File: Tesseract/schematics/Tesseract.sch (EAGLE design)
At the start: 108 parts, among them IC1 MC7805CDTG, IC2 QUAD_OPAMPD, IC3 NE5532D, IC4 LM4040B10, IC5 NE5532D, Q1 SI2309CDS, Q2 BSS123, Q901 BC846

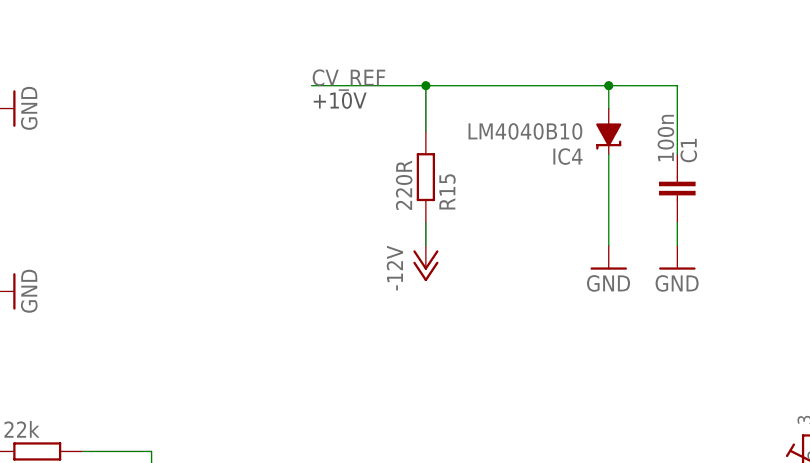
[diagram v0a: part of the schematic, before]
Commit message: changed current limiting vref resistor value to 150R
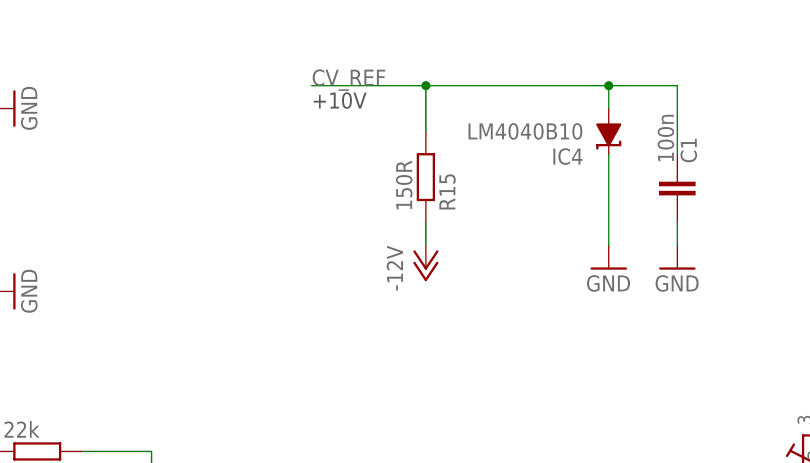
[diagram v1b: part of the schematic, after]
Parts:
- R15: value 220R -> 150R
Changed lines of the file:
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@@
 <part name="GND17" library="supply1" deviceset="GND" device=""/>
 <part name="P-2" library="supply1" deviceset="-12V" device=""/>
-<part name="R15" library="Rebel" deviceset="R-EU_" device="0603" value="220R"/>
+<part name="R15" library="Rebel" deviceset="R-EU_" device="0603" value="150R"/>
 <part name="C1" library="resistor" deviceset="C-EU" device="C0603" value="100n"/>
 <part name="GND18" library="supply1" deviceset="GND" device=""/>

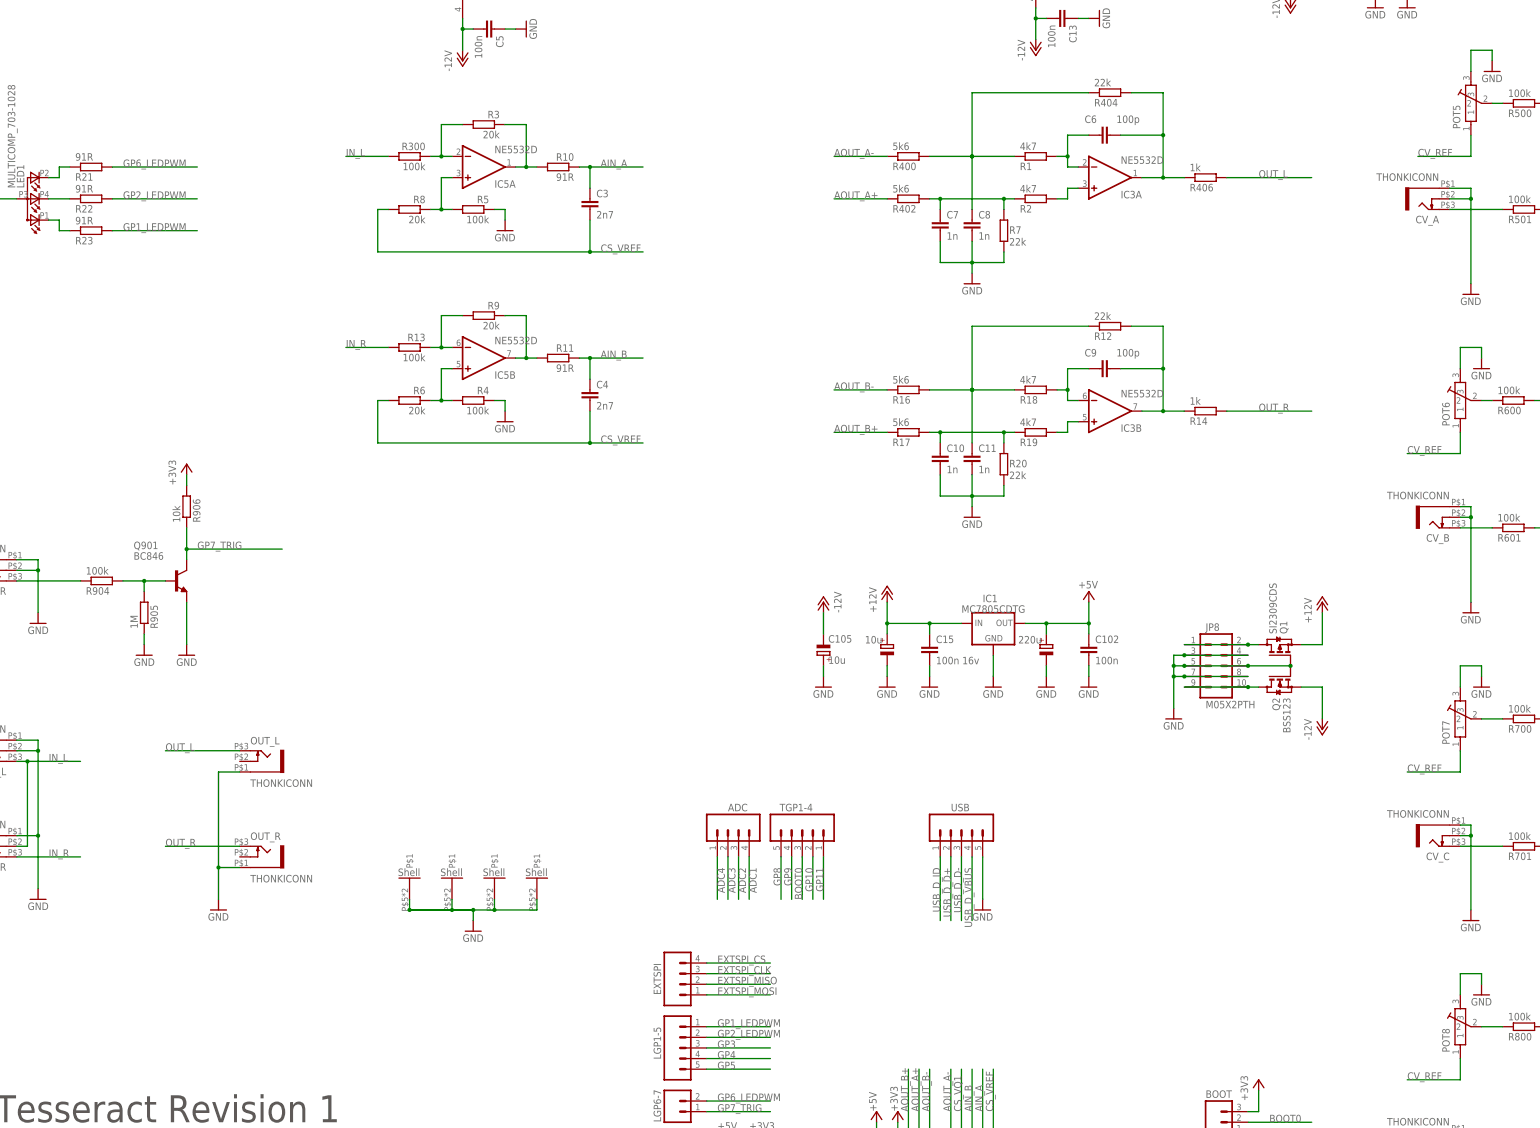
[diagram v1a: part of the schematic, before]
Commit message: component value and name changes
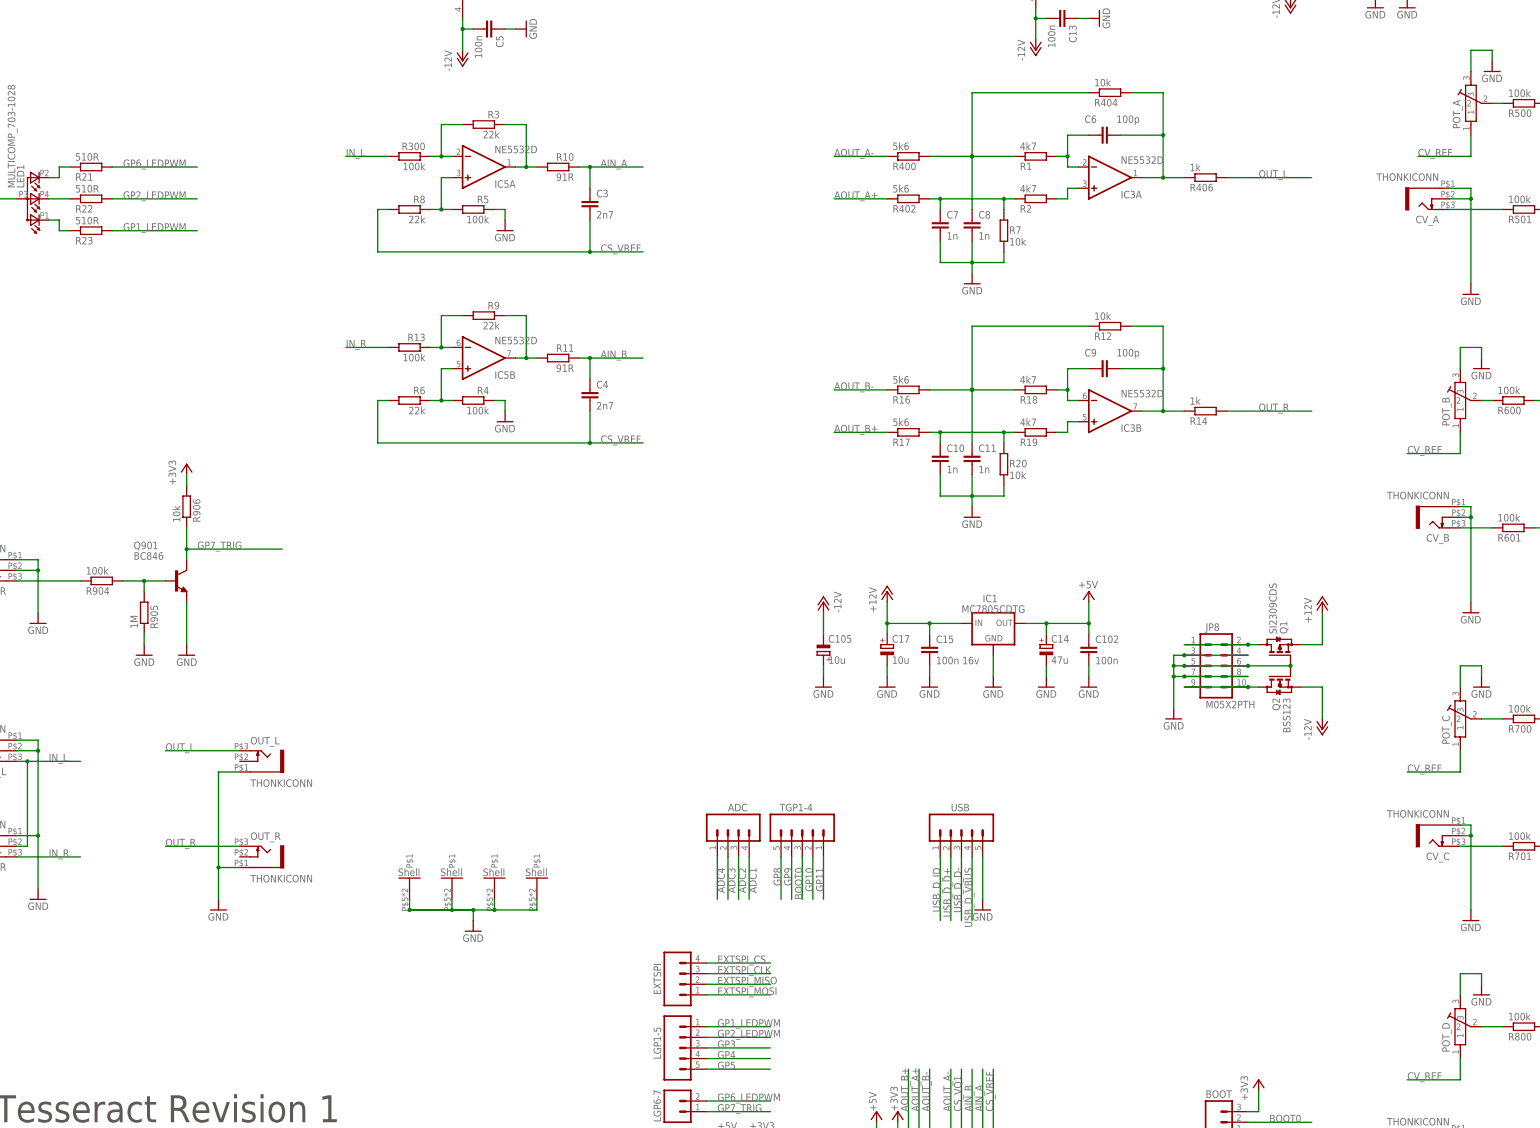
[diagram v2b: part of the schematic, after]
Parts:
- C14: value 220u -> 47u
- R12, R20, R404, R7: value 22k -> 10k
- R21, R22, R23: value 91R -> 510R
- R3, R6, R8, R9: value 20k -> 22k
- renumbered POT5 to POT_A, POT6 to POT_B, POT7 to POT_C, POT8 to POT_D

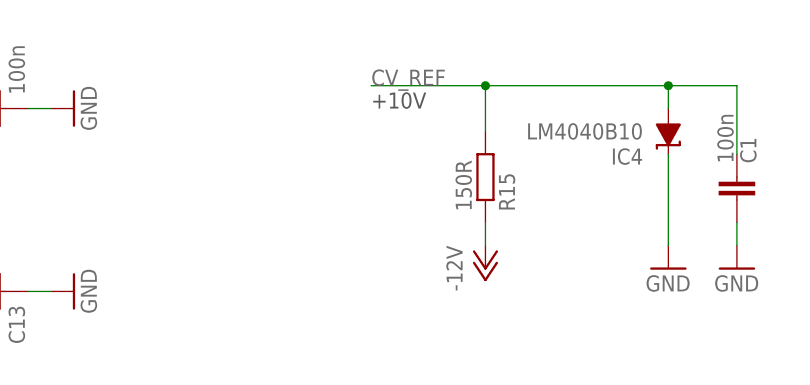
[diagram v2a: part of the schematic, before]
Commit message: corrected vref label
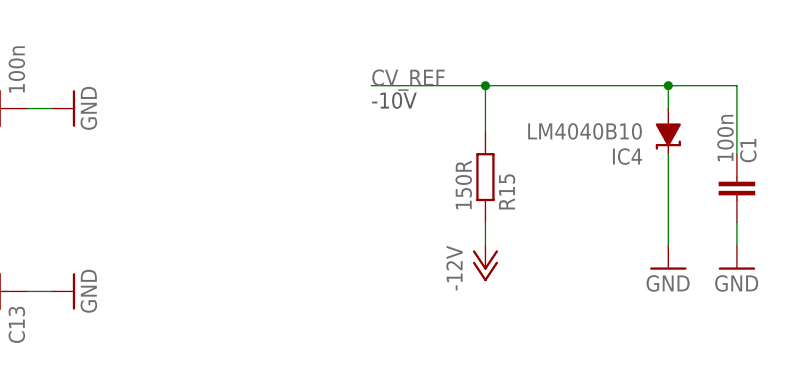
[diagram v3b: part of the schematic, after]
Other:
- note added: "-10V"
- note removed: "+10V"
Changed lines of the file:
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@@
 <text x="-66.04" y="-30.48" size="3.81" layer="97" font="vector">Copyright 2017 Rebel Technology</text>
 <text x="-66.04" y="-38.1" size="3.81" layer="97" font="vector">Published under the GNU GPL</text>
-<text x="231.14" y="261.62" size="1.778" layer="97">+10V</text>
+<text x="231.14" y="261.62" size="1.778" layer="97">-10V</text>
 </plain>
 <instances>

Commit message: rev02 changes
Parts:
- removed C105: 10u, resistor:CPOL-EUA
- added C18: 10u, Rebel:CPOL-EU153CLV-0505
- C17: device resistor:CPOL-EUA -> Rebel:CPOL-EU153CLV-0505
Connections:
- net -12V: now also C18.-; no longer C105.-
- net GND: now also C18.+; no longer C105.+
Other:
- note added: "Tesseract Rev02"
- note removed: "Tesseract Revision 1"
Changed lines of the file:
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@@
 <part name="GND48" library="supply1" deviceset="GND" device=""/>
 <part name="D800" library="diode" deviceset="BAT54S" device=""/>
-<part name="C105" library="resistor" deviceset="CPOL-EU" device="A" value="10u"/>
+<part name="C18" library="Rebel" deviceset="CPOL-EU" device="153CLV-0505" value="10u"/>
 <part name="C501" library="resistor" deviceset="C-EU" device="C0603" value="100n"/>
 <part name="GND54" library="supply1" deviceset="GND" device=""/>
@@
 <part name="P+14" library="supply1" deviceset="+12V" device=""/>
 <part name="P+6" library="supply1" deviceset="+5V" device=""/>
-<part name="C17" library="resistor" deviceset="CPOL-EU" device="A" value="10u"/>
+<part name="C17" library="Rebel" deviceset="CPOL-EU" device="153CLV-0505" value="10u"/>
 <part name="C14" library="rcl" deviceset="CPOL-EU" device="C" value="47u"/>
 <part name="LED1" library="Rebel" deviceset="MULTICOMP_703-1028" device=""/>
@@
 <sheet>
 <plain>
-<text x="-66.04" y="-22.86" size="6.4516" layer="97" font="vector">Tesseract Revision 1</text>
+<text x="-66.04" y="-22.86" size="6.4516" layer="97" font="vector">Tesseract Rev02</text>
 <text x="-66.04" y="-30.48" size="3.81" layer="97" font="vector">Copyright 2017 Rebel Technology</text>
 <text x="-66.04" y="-38.1" size="3.81" layer="97" font="vector">Published under the GNU GPL</text>
@@
 <instance part="GND48" gate="1" x="345.44" y="-48.26" rot="MR0"/>
 <instance part="D800" gate="G$1" x="353.06" y="-43.18"/>
-<instance part="C105" gate="G$1" x="132.08" y="88.9" smashed="yes" rot="R180">
+<instance part="C18" gate="G$1" x="132.08" y="88.9" smashed="yes" rot="R180">
 <attribute name="NAME" x="133.223" y="91.9226" size="1.778" layer="95"/>
 <attribute name="VALUE" x="133.223" y="86.8426" size="1.778" layer="96"/>
@@
 <pinref part="GND52" gate="1" pin="GND"/>
 <wire x1="132.08" y1="83.82" x2="132.08" y2="86.36" width="0.1524" layer="91"/>
-<pinref part="C105" gate="G$1" pin="+"/>
+<pinref part="C18" gate="G$1" pin="+"/>
 </segment>
 <segment>
@@
 <pinref part="P-10" gate="1" pin="-12V"/>
 <wire x1="132.08" y1="93.98" x2="132.08" y2="99.06" width="0.1524" layer="91"/>
-<pinref part="C105" gate="G$1" pin="-"/>
-</segment>
-<segment>
+<pinref part="C18" gate="G$1" pin="-"/>
+</segment>
+<segment>
